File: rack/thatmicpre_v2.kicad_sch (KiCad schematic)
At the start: 81 parts

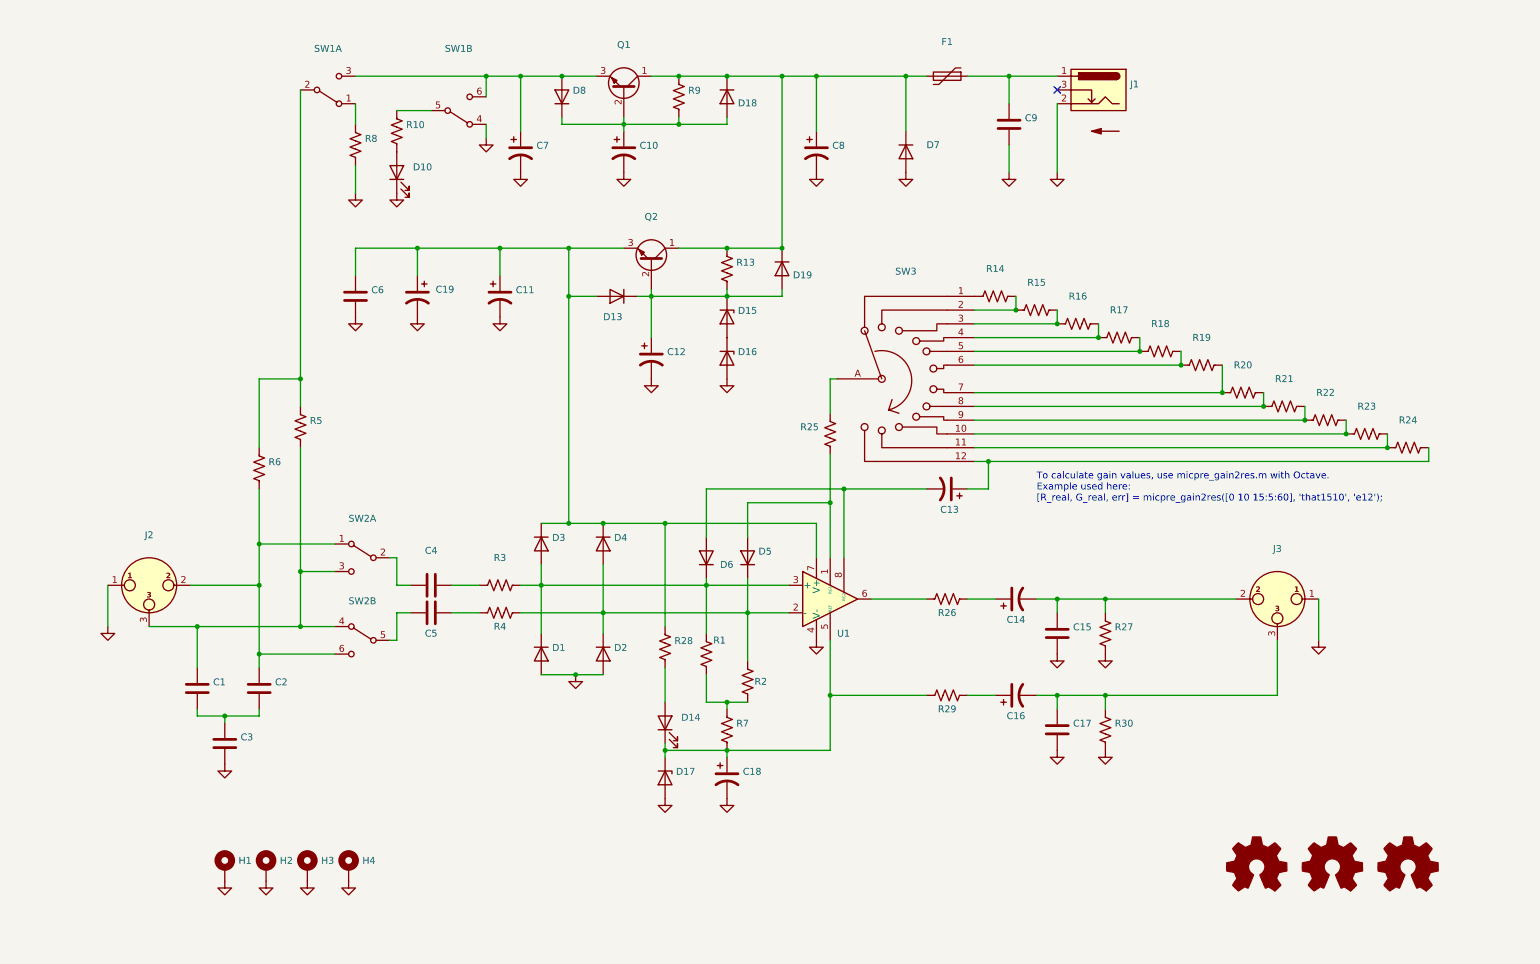
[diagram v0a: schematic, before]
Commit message: First complete layout of v2
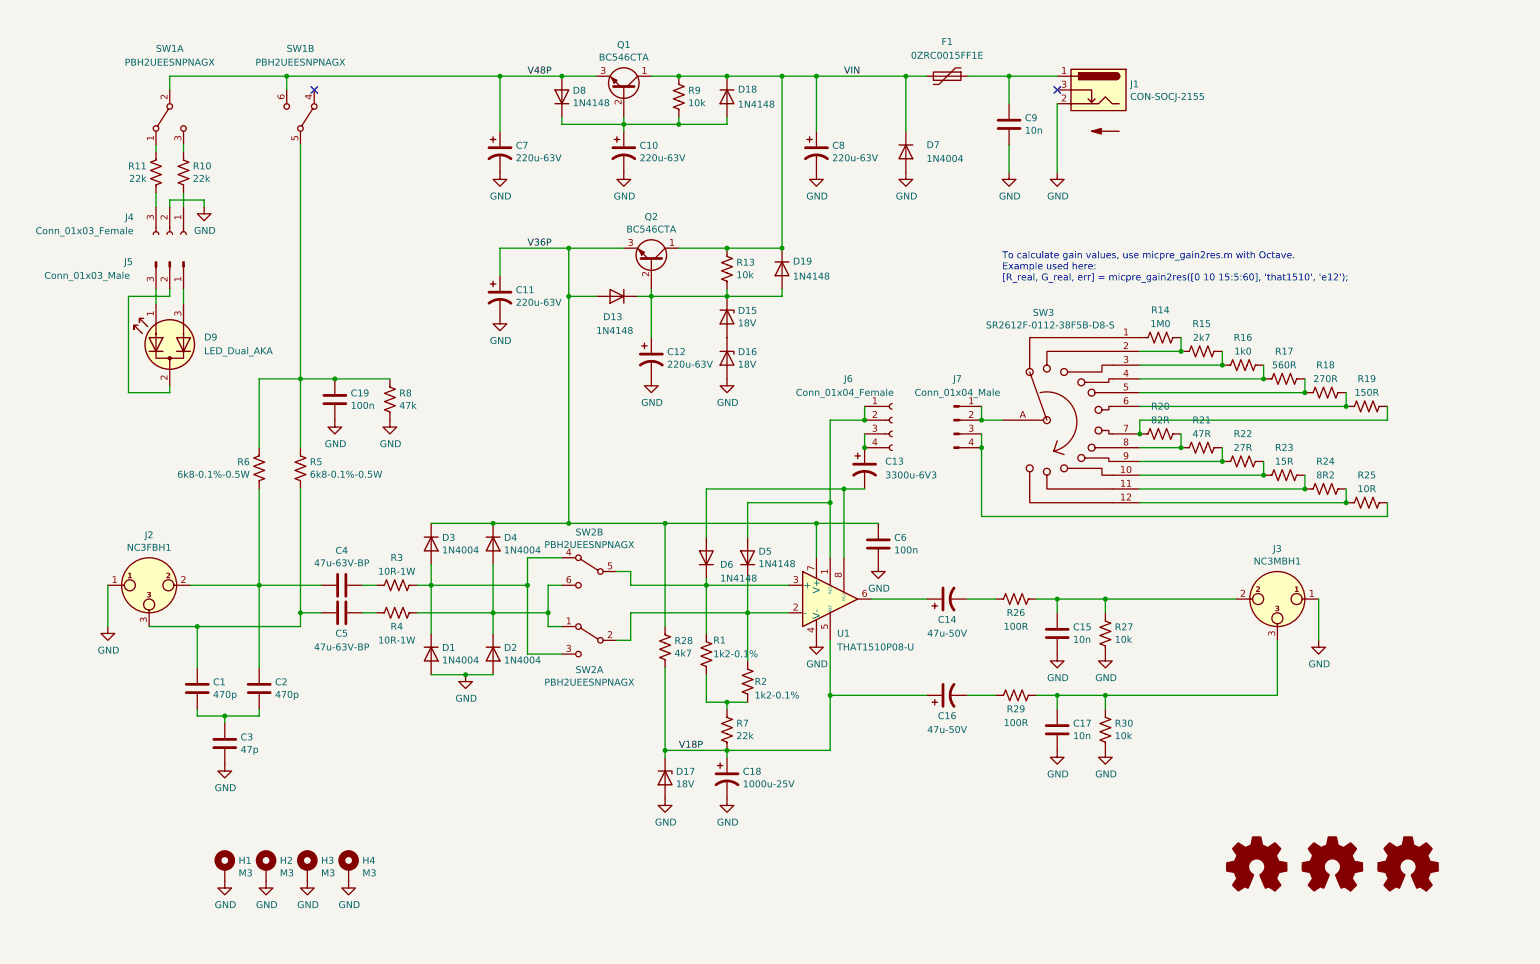
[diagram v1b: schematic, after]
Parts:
- removed C19: (no value), symbol Device:C_Polarized_US
- removed D10, D14: (no value), symbol Device:LED
- added C19: 100n, Capacitor_THT:C_Rect_L7.2mm_W3.0mm_P5.00mm_FKS2_FKP2_MKS2_MKP2, symbol Device:C
- added D9: LED_Dual_AKA, LED_THT:LED_D5.0mm-3, symbol Device:LED_Dual_AKA
- added J4: Conn_01x03_Female, Connector_PinSocket_2.54mm:PinSocket_1x03_P2.54mm_Horizontal, symbol Connector:Conn_01x03_Female
- added J5: Conn_01x03_Male, Connector_PinHeader_2.54mm:PinHeader_1x03_P2.54mm_Vertical, symbol Connector:Conn_01x03_Male
- added J6: Conn_01x04_Female, Connector_PinSocket_2.54mm:PinSocket_1x04_P2.54mm_Horizontal, symbol Connector:Conn_01x04_Female
- added J7: Conn_01x04_Male, Connector_PinHeader_2.54mm:PinHeader_1x04_P2.54mm_Vertical, symbol Connector:Conn_01x04_Male
- added R11: 22k, Resistor_THT:R_Axial_DIN0207_L6.3mm_D2.5mm_P10.16mm_Horizontal, symbol Device:R_US
- C1, C2: value (none) -> 470p; footprint (none) -> Capacitor_THT:C_Disc_D5.0mm_W2.5mm_P5.00mm
- C10, C12, C7, C8: value (none) -> 220u-63V; footprint (none) -> Capacitor_THT:CP_Radial_D10.0mm_P5.00mm
- C11: value (none) -> 220u-63V; footprint (none) -> Capacitor_THT:CP_Radial_D10.0mm_P5.00mm; Vendor UFW1H470MED1TD -> UPW1J221MPD
- C13: value (none) -> 3300u-6V3; footprint (none) -> Capacitor_THT:CP_Radial_D10.0mm_P5.00mm
- C14, C16: value (none) -> 47u-50V; footprint (none) -> Capacitor_THT:CP_Radial_D6.3mm_P2.50mm
- C15, C17, C9: value (none) -> 10n; footprint (none) -> Capacitor_THT:C_Rect_L7.2mm_W3.0mm_P5.00mm_FKS2_FKP2_MKS2_MKP2
- C18: value (none) -> 1000u-25V; footprint (none) -> Capacitor_THT:CP_Radial_D10.0mm_P5.00mm
- C3: value (none) -> 47p; footprint (none) -> Capacitor_THT:C_Disc_D5.0mm_W2.5mm_P5.00mm
- C4, C5: value (none) -> 47u-63V-BP; footprint (none) -> Capacitor_THT:C_Radial_D10.0mm_H16.0mm_P5.00mm
- C6: value (none) -> 100n; footprint (none) -> Capacitor_THT:C_Rect_L7.2mm_W3.0mm_P5.00mm_FKS2_FKP2_MKS2_MKP2
- D1, D2, D3, D4, D7: value (none) -> 1N4004; footprint (none) -> Diode_THT:D_DO-41_SOD81_P10.16mm_Horizontal
- D13, D18, D19, D5, D6, D8: value (none) -> 1N4148; footprint (none) -> Diode_THT:D_DO-34_SOD68_P7.62mm_Horizontal
- D15, D16, D17: value (none) -> 18V; footprint (none) -> Diode_THT:D_DO-34_SOD68_P7.62mm_Horizontal
- F1: value (none) -> 0ZRC0015FF1E; footprint (none) -> Fuse:Fuse_BelFuse_0ZRE0005FF_L8.3mm_W3.8mm; Vendor 0ZRC0015FF1E -> Bel Fuse
- H1, H2, H3, H4: value (none) -> M3; footprint (none) -> MountingHole:MountingHole_3.2mm_M3_Pad
- J1: value (none) -> CON-SOCJ-2155; footprint (none) -> Connector_BarrelJack:BarrelJack_Horizontal; Vendor CON-SOCJ-2155 -> (none)
- J2: value (none) -> NC3FBH1; footprint (none) -> Connector_Audio:Jack_XLR_Neutrik_NC3FBH1_Horizontal; Vendor NC3FBH1 -> Neutrik
- J3: value (none) -> NC3MBH1; footprint (none) -> Connector_Audio:Jack_XLR_Neutrik_NC3MBH_Horizontal; Vendor NC3MBH -> Neutrik
- LOGO1: value (none) -> Logo_Open_Hardware_Small; footprint (none) -> Symbol:OSHW-Symbol_6.7x6mm_Copper
- LOGO2: value (none) -> Logo_Open_Hardware_Small; footprint (none) -> Symbol:Symbol_CC-Attribution_CopperTop_Small
- LOGO3: value (none) -> Logo_Open_Hardware_Small; footprint (none) -> Symbol:Symbol_CreativeCommons_CopperTop_Type2_Small
- LOGO4: value (none) -> SYM_Arrow_Normal; footprint (none) -> Symbol:Symbol_Barrel_Polarity
- Q1: value (none) -> BC546CTA; footprint (none) -> Package_TO_SOT_THT:TO-92_Inline_Wide; Cmp name (none) -> BC546CTA
- Q2: value (none) -> BC546CTA; footprint (none) -> Package_TO_SOT_THT:TO-92_Inline_Wide
- R1, R2: value (none) -> 1k2-0.1%; footprint (none) -> Resistor_THT:R_Axial_DIN0207_L6.3mm_D2.5mm_P10.16mm_Horizontal
- R10, R7: value (none) -> 22k; footprint (none) -> Resistor_THT:R_Axial_DIN0207_L6.3mm_D2.5mm_P10.16mm_Horizontal
- R13, R27, R30, R9: value (none) -> 10k; footprint (none) -> Resistor_THT:R_Axial_DIN0207_L6.3mm_D2.5mm_P10.16mm_Horizontal
- R14: value (none) -> 1M0; footprint (none) -> Resistor_THT:R_Axial_DIN0207_L6.3mm_D2.5mm_P10.16mm_Horizontal
- R15: value (none) -> 2k7; footprint (none) -> Resistor_THT:R_Axial_DIN0207_L6.3mm_D2.5mm_P10.16mm_Horizontal
- R16: value (none) -> 1k0; footprint (none) -> Resistor_THT:R_Axial_DIN0207_L6.3mm_D2.5mm_P10.16mm_Horizontal
- R17: value (none) -> 560R; footprint (none) -> Resistor_THT:R_Axial_DIN0207_L6.3mm_D2.5mm_P10.16mm_Horizontal
- R18: value (none) -> 270R; footprint (none) -> Resistor_THT:R_Axial_DIN0207_L6.3mm_D2.5mm_P10.16mm_Horizontal
- R19: value (none) -> 150R; footprint (none) -> Resistor_THT:R_Axial_DIN0207_L6.3mm_D2.5mm_P10.16mm_Horizontal
- R20: value (none) -> 82R; footprint (none) -> Resistor_THT:R_Axial_DIN0207_L6.3mm_D2.5mm_P10.16mm_Horizontal
- R21: value (none) -> 47R; footprint (none) -> Resistor_THT:R_Axial_DIN0207_L6.3mm_D2.5mm_P10.16mm_Horizontal
- R22: value (none) -> 27R; footprint (none) -> Resistor_THT:R_Axial_DIN0207_L6.3mm_D2.5mm_P10.16mm_Horizontal
- R23: value (none) -> 15R; footprint (none) -> Resistor_THT:R_Axial_DIN0207_L6.3mm_D2.5mm_P10.16mm_Horizontal
- R24: value (none) -> 8R2; footprint (none) -> Resistor_THT:R_Axial_DIN0207_L6.3mm_D2.5mm_P10.16mm_Horizontal
- R25: value (none) -> 10R; footprint (none) -> Resistor_THT:R_Axial_DIN0207_L6.3mm_D2.5mm_P10.16mm_Horizontal
- R26, R29: value (none) -> 100R; footprint (none) -> Resistor_THT:R_Axial_DIN0207_L6.3mm_D2.5mm_P10.16mm_Horizontal
- R28: value (none) -> 4k7; footprint (none) -> Resistor_THT:R_Axial_DIN0207_L6.3mm_D2.5mm_P10.16mm_Horizontal
- R3, R4: value (none) -> 10R-1W; footprint (none) -> Resistor_THT:R_Axial_DIN0207_L6.3mm_D2.5mm_P10.16mm_Horizontal
- R5, R6: value (none) -> 6k8-0.1%-0.5W; footprint (none) -> Resistor_THT:R_Axial_DIN0207_L6.3mm_D2.5mm_P10.16mm_Horizontal
- R8: value (none) -> 47k; footprint (none) -> Resistor_THT:R_Axial_DIN0207_L6.3mm_D2.5mm_P10.16mm_Horizontal
- SW1, SW2: value (none) -> PBH2UEESNPNAGX; footprint (none) -> my_kicad_footprints:SW_PBH2UEESNPNAGX; Vendor 200MDP1T2B2M6QE -> E-Switch
- SW3: value (none) -> SR2612F-0112-38F5B-D8-S; footprint (none) -> my_kicad_footprints:LORINCK1049; Vendor SR2612F-0112-38F5B-D8-S -> Alpha
- U1: value (none) -> THAT1510P08-U; footprint (none) -> Package_DIP:DIP-8_W7.62mm; Vendor THAT1510P08-U -> THAT Corp
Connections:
- net GND: now also C19.2, J4.2 (Pin_2); no longer SW1.4 (A)
- net at D5.2 (A), U1.1 (RG1): now also J6.1 (Pin_1), J6.2 (Pin_2); no longer R25.1
- net at D5.1 (K), R2.1, U1.2 (-): now also SW2.2 (B); no longer D2.1 (K), D4.2 (A), R4.1
- net at D6.1 (K), R1.1, U1.3 (+): now also SW2.5 (B); no longer D1.1 (K), D3.2 (A), R3.1
- net V18P: now reaches C18.1, D17.1 (K), R7.2, U1.5 (REF)
- net V18P: now also C16.1, R28.2; no longer R29.2
- net at U1.6: now also C14.1; no longer R26.2
- net V36P: now reaches C11.1, C6.1, D13.2 (A), D3.1 (K), D4.1 (K), Q2.3 (E), R28.1, U1.7 (V+)
- net at R5.1, R6.1: now also R8.1, SW1.5 (B), C19.1; no longer SW1.2 (B)
- net at C2.1, J2.2, R6.2: now also C4.1; no longer SW2.1 (A), SW2.6 (C)
- net at C1.1, J2.3, R5.2: now also C5.1; no longer SW2.3 (C), SW2.4 (A)
- net at R10.1: now also SW1.3 (C); no longer SW1.5 (B)
- net at R10.2: now also J4.1 (Pin_1)
- net VIN: now reaches C8.1, D18.1 (K), D19.1 (K), D7.1 (K), F1.2, Q1.1 (C), Q2.1 (C), R13.1, R9.1
- net V48P: now reaches C7.1, D8.2 (A), Q1.3 (E)
- net V48P: now also SW1.2 (B), SW1.6 (C); no longer SW1.3 (C), SW1.6 (C)
- net at C15.1, J3.2, R27.1: now also R26.1; no longer C14.2
- net at C17.1, J3.3, R30.1: now also R29.1; no longer C16.2
- net at R24.1, SW3.12: now also R25.1; no longer C13.1
- net at R25.2: now also J7.3 (Pin_3), J7.4 (Pin_4); no longer SW3.A
- new net: D2.1 (K), D4.2 (A), R4.1, SW2.1 (A), SW2.6 (C)
- new net: D1.1 (K), D3.2 (A), R3.1, SW2.3 (C), SW2.4 (A)
- new net: C14.2, R26.2
- new net: C16.2, R29.2
- new net: C13.1, J6.3 (Pin_3), J6.4 (Pin_4)
- new net: J7.1 (Pin_1), J7.2 (Pin_2), SW3.A
- new net: R11.1, SW1.1 (A)
- new net: D9.3 (A2), J5.1 (Pin_1)
- new net: D9.2 (K), J5.2 (Pin_2)
- new net: D9.1 (A1), J5.3 (Pin_3)
- new net: J4.3 (Pin_3), R11.2
- no-connect marks 1 -> 2
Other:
- moved on the sheet: C13, C14, C16, C4, C5, C6, C7, D1, D2, D3, D4, R10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

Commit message: Redo power section layout, add PSU option
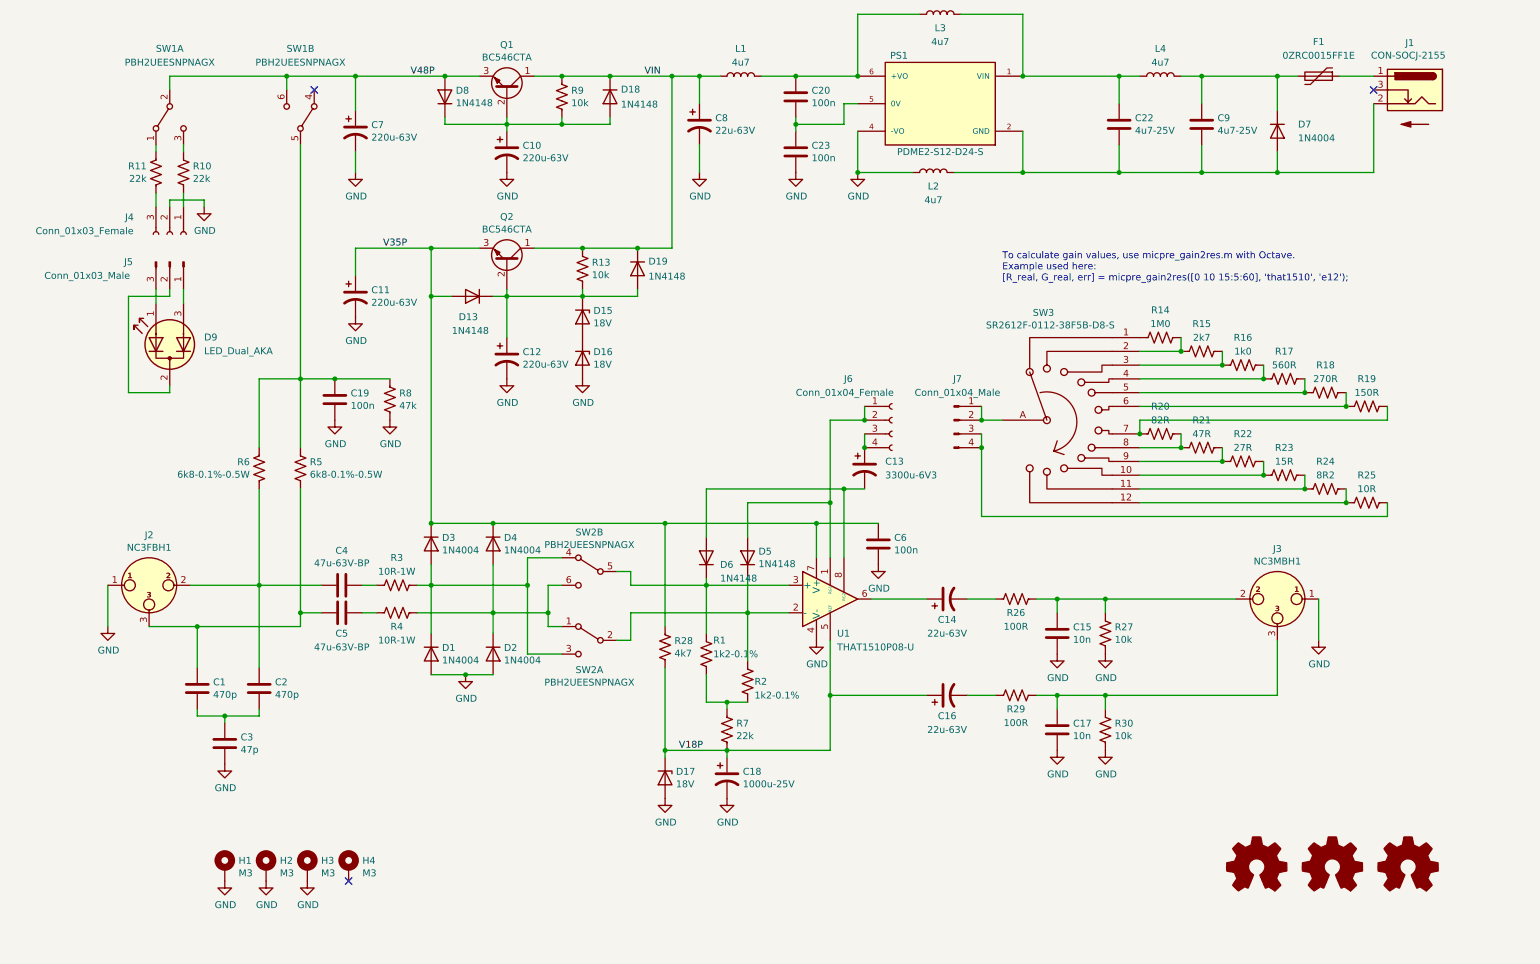
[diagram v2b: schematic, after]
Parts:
- added C20, C23: 100n, Capacitor_THT:C_Rect_L7.2mm_W3.0mm_P5.00mm_FKS2_FKP2_MKS2_MKP2, symbol Device:C
- added C22: 4u7-25V, Capacitor_THT:C_Rect_L7.2mm_W3.0mm_P5.00mm_FKS2_FKP2_MKS2_MKP2, symbol Device:C
- added L1, L2, L3, L4: 4u7, Inductor_THT:L_Axial_L5.3mm_D2.2mm_P10.16mm_Horizontal_Vishay_IM-1, symbol Device:L
- added PS1: PDME2-S12-D24-S, CONV_PDME2-S12-D24-S, symbol PDME2-S12-D24-S:PDME2-S12-D24-S
- C14, C16: value 47u-50V -> 22u-63V; Vendor UFW1H470MED1TD -> (none)
- C8: value 220u-63V -> 22u-63V; footprint Capacitor_THT:CP_Radial_D10.0mm_P5.00mm -> Capacitor_THT:CP_Radial_D6.3mm_P2.50mm; Vendor UPW1J221MPD -> (none)
- C9: value 10n -> 4u7-25V; Vendor PHE426DJ5100JR05 -> FG28X5R1E475KRT06
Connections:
- net GND: now also C23.2, L2.1, PS1.4 (-VO); no longer C9.2, D7.2 (A), H4.1, J1.2
- net VIN: now also L1.1; no longer D7.1 (K), F1.2
- net at F1.1, J1.1: no longer C9.1
- net V36P renamed V35P
- new net: C9.1, D7.1 (K), F1.2, L4.2
- new net: C22.2, C9.2, D7.2 (A), J1.2, L2.2, PS1.2 (GND)
- new net: C20.2, C23.1, PS1.5 (0V)
- new net: C22.1, L3.2, L4.1, PS1.1 (VIN)
- new net: C20.1, L1.2, L3.1, PS1.6 (+VO)
- no-connect marks 2 -> 3
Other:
- moved on the sheet: C10, C11, C12, C7, D13, D15, D16, D18, D19, D7, D8, F1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

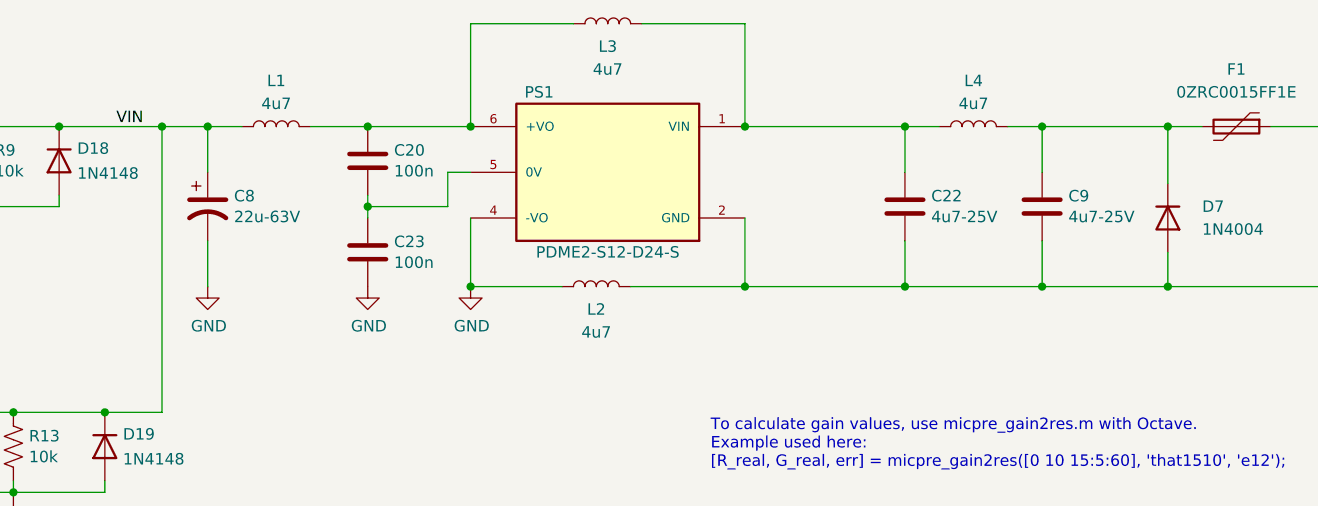
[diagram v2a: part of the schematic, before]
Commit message: Remove PSU option
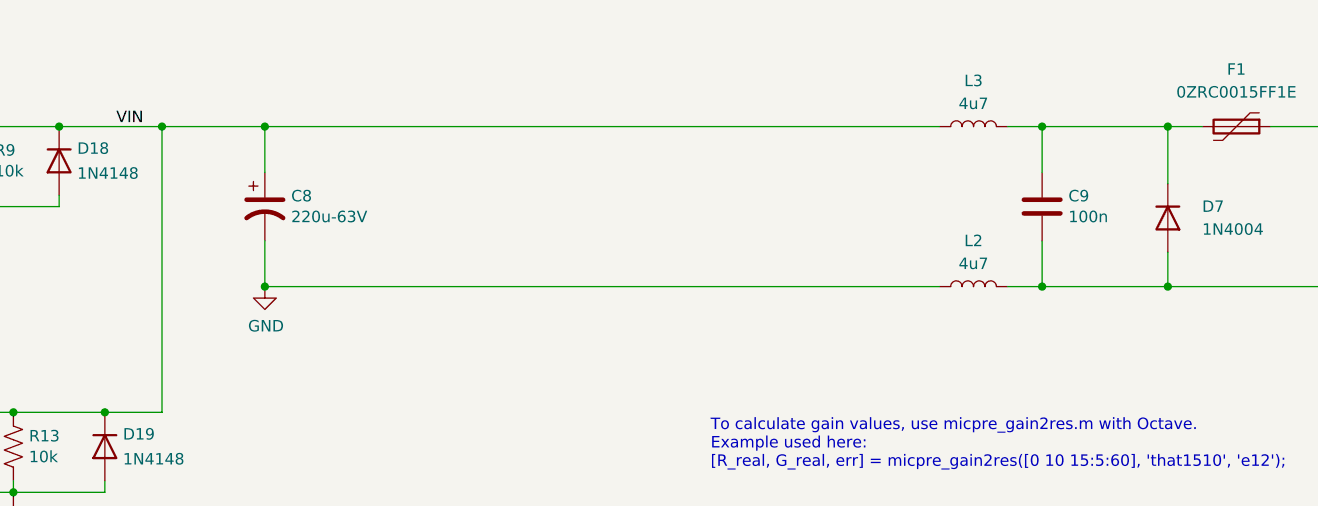
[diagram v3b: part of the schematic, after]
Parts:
- removed C20, C23: 100n, Capacitor_THT:C_Rect_L7.2mm_W3.0mm_P5.00mm_FKS2_FKP2_MKS2_MKP2, symbol Device:C
- removed C22: 4u7-25V, Capacitor_THT:C_Rect_L7.2mm_W3.0mm_P5.00mm_FKS2_FKP2_MKS2_MKP2, symbol Device:C
- removed L1, L3: 4u7, Inductor_THT:L_Axial_L5.3mm_D2.2mm_P10.16mm_Horizontal_Vishay_IM-1, symbol Device:L
- removed PS1: PDME2-S12-D24-S, CONV_PDME2-S12-D24-S, symbol PDME2-S12-D24-S:PDME2-S12-D24-S
- C8: value 22u-63V -> 220u-63V; footprint Capacitor_THT:CP_Radial_D6.3mm_P2.50mm -> Capacitor_THT:CP_Radial_D10.0mm_P5.00mm; Vendor (none) -> UPW1J221MPD
- C9: value 4u7-25V -> 100n
- renumbered L4 to L3
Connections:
- net VIN: now also L3.1

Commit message: optimized layout
added alternative jack and headers
checked against prints for mech fit
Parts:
- removed C19: 100n, Capacitor_THT:C_Rect_L7.2mm_W3.0mm_P5.00mm_FKS2_FKP2_MKS2_MKP2, symbol Device:C
- added J10: Conn_01x03_Female, Connector_PinHeader_2.54mm:PinHeader_1x03_P2.54mm_Vertical, symbol Connector:Conn_01x03_Female
- added J8: Conn_01x04_Female, Connector_PinHeader_2.54mm:PinHeader_1x04_P2.54mm_Vertical, symbol Connector:Conn_01x04_Female
- added J9: NMJ6HFD2, Connector_Audio:Jack_6.35mm_Neutrik_NMJ6HFD2_Horizontal, symbol Connector:AudioJack3_Switch
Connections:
- net GND: now also J10.2 (Pin_2), J9.S
- net at D5.2 (A), U1.1 (RG1): now also C13.2; no longer J6.1 (Pin_1), J6.2 (Pin_2)
- net at D6.2 (A), U1.8 (RG2): now also J6.3 (Pin_3), J6.4 (Pin_4), J8.1 (Pin_1), J8.2 (Pin_2); no longer C13.2
- net at J4.1 (Pin_1), R10.2: now also J10.1 (Pin_1)
- net at C15.1, J3.2, R26.1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: now also J9.T
- net at C17.1, J3.3, R29.1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: now also J9.R
- net at J4.3 (Pin_3), R11.2: now also J10.3 (Pin_3)
- new net: C13.1, J6.1 (Pin_1), J6.2 (Pin_2), J8.3 (Pin_3), J8.4 (Pin_4)
- no-connect marks 3 -> 6
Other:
- moved on the sheet: C13, C4, C5, C8, C9, D7, F1, J1, L2, L3, R10, R11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
